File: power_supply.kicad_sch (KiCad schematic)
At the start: 27 parts, among them U7 LM2733XMF

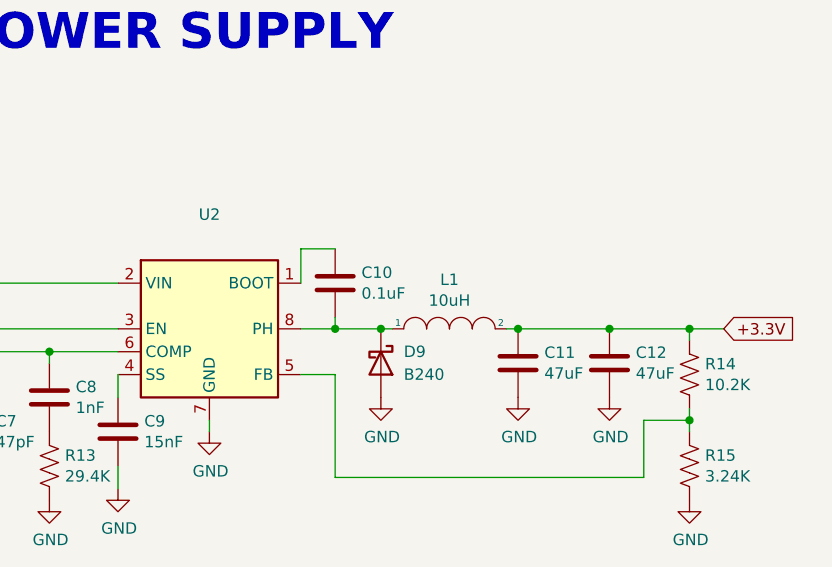
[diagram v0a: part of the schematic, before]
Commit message: Added connector for temperature sensor. Started to route board.
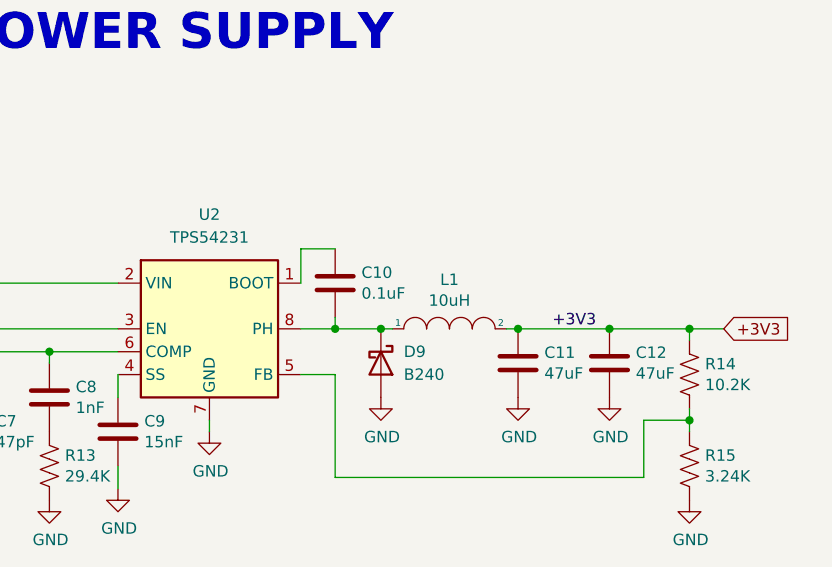
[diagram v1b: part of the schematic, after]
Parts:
- U2: value (none) -> TPS54231; footprint (none) -> Package_SO:SOIC-8_3.9x4.9mm_P1.27mm
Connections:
- net +3.3V renamed +3V3
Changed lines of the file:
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@@
     (effects (font (size 3.9878 3.9878) (thickness 0.7976) bold) (justify left bottom))
   )
-  (global_label "+3.3V" (shape input) (at 209.55 60.96 0) (fields_autoplaced)
+  (label "+3V3" (at 190.5 60.96 0)
+    (effects (font (size 1.27 1.27)) (justify left bottom))
+  )
+  (global_label "+3V3" (shape input) (at 209.55 60.96 0) (fields_autoplaced)
     (effects (font (size 1.27 1.27)) (justify left))
-    (property "Intersheet References" "${INTERSHEET_REFS}" (id 0) (at -6.35 -21.59 0)
-      (effects (font (size 1.27 1.27)) hide)
+    (property "Intersheet References" "${INTERSHEET_REFS}" (id 0) (at 216.9542 60.8806 0)
+      (effects (font (size 1.27 1.27)) (justify left) hide)
     )
   )
@@
     (in_bom yes) (on_board yes) (fields_autoplaced)
     (property "Reference" "U2" (id 0) (at 152.4 48.26 0))
-    (property "Value" "" (id 1) (at 152.4 50.8 0))
-    (property "Footprint" "" (id 2) (at 152.4 60.96 0)
-      (effects (font (size 1.27 1.27)) hide)
-    )
+    (property "Value" "TPS54231" (id 1) (at 152.4 50.8 0))
+    (property "Footprint" "Package_SO:SOIC-8_3.9x4.9mm_P1.27mm" (id 2) (at 152.4 60.96 0)
+      (effects (font (size 1.27 1.27)) hide)
+    )

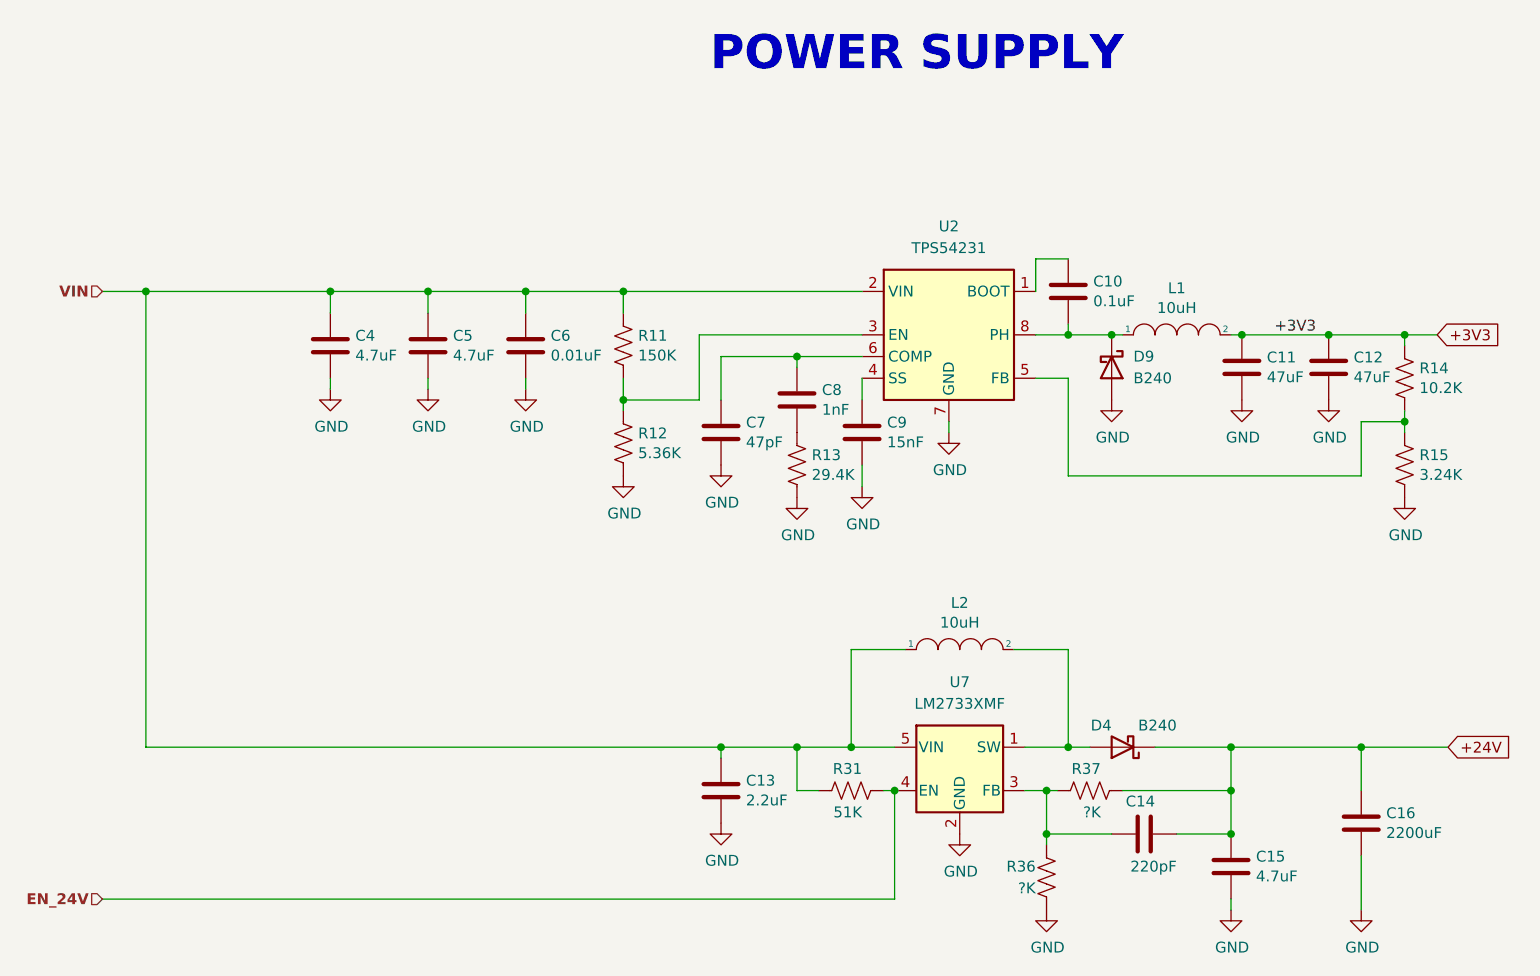
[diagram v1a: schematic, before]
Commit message: Added clamping diode for 24V net.
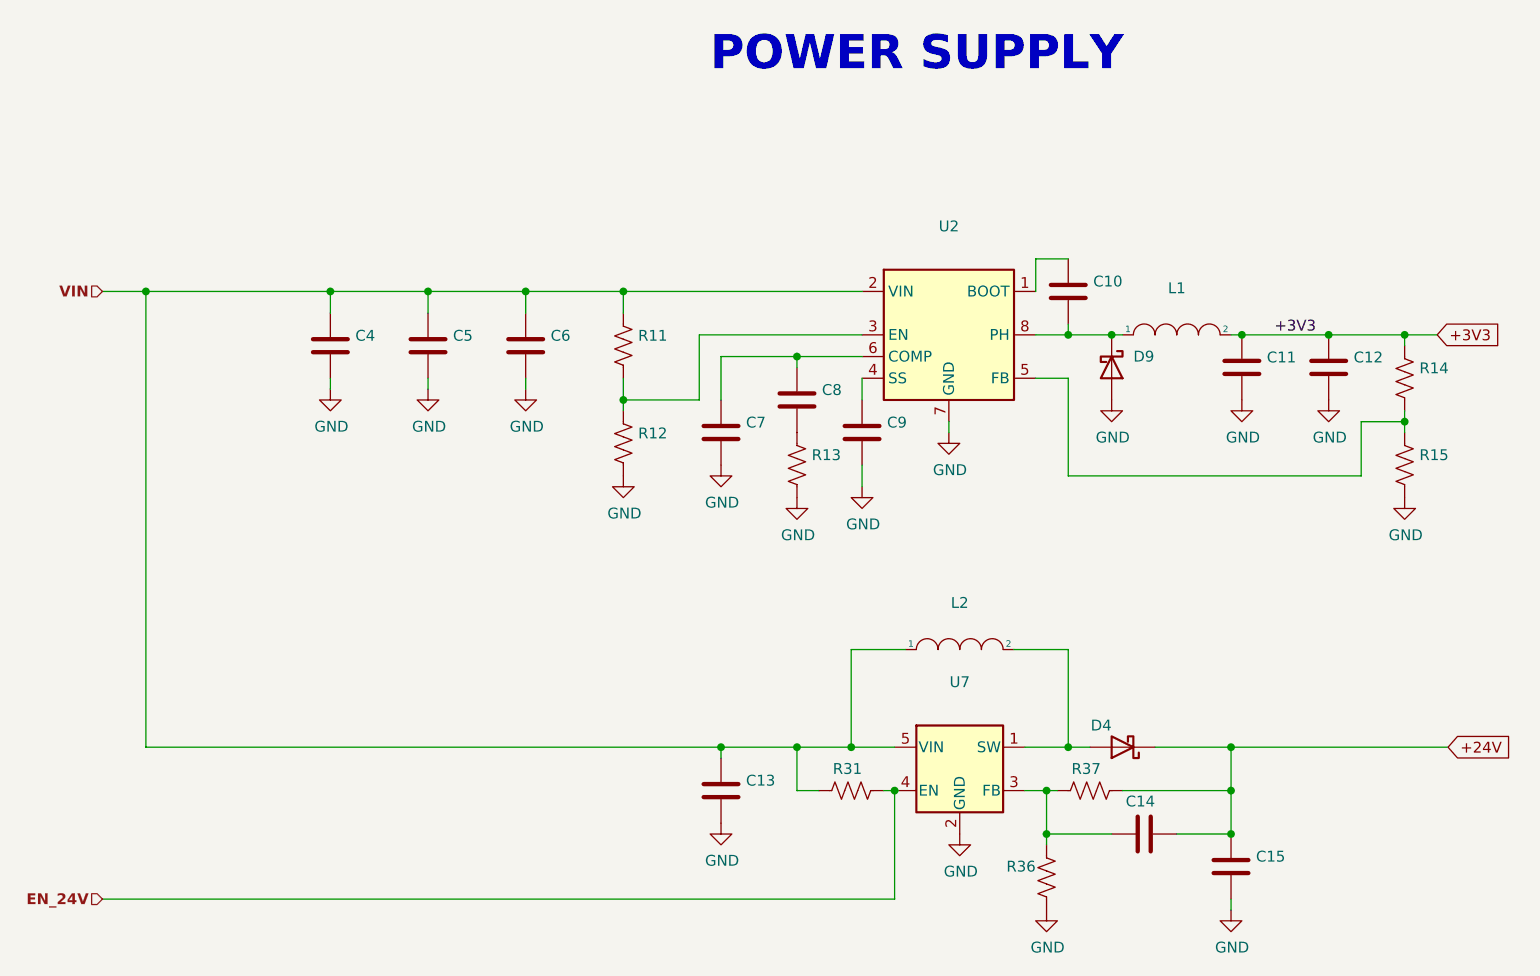
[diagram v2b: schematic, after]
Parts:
- removed C16: 2200uF, Capacitor_SMD:C_0805_2012Metric, symbol Device:C
- C10: value 0.1uF -> (none); footprint Capacitor_SMD:C_0805_2012Metric -> (none)
- C11, C12: value 47uF -> (none); footprint Capacitor_SMD:C_0805_2012Metric -> (none)
- C13: value 2.2uF -> (none); footprint Capacitor_SMD:C_0805_2012Metric -> (none)
- C14: value 220pF -> (none); footprint Capacitor_SMD:C_0805_2012Metric -> (none)
- C15, C4, C5: value 4.7uF -> (none); footprint Capacitor_SMD:C_0805_2012Metric -> (none)
- C6: value 0.01uF -> (none); footprint Capacitor_SMD:C_0805_2012Metric -> (none)
- C7: value 47pF -> (none); footprint Capacitor_SMD:C_0805_2012Metric -> (none)
- C8: value 1nF -> (none); footprint Capacitor_SMD:C_0805_2012Metric -> (none)
- C9: value 15nF -> (none); footprint Capacitor_SMD:C_0805_2012Metric -> (none)
- D4, D9: value B240 -> (none); footprint Diode_SMD:D_SMB -> (none)
- L1, L2: value 10uH -> (none); footprint Inductor_SMD:L_Taiyo-Yuden_NR-50xx -> (none)
- R11: value 150K -> (none); footprint Resistor_SMD:R_0805_2012Metric -> (none)
- R12: value 5.36K -> (none); footprint Resistor_SMD:R_0805_2012Metric -> (none)
- R13: value 29.4K -> (none); footprint Resistor_SMD:R_0805_2012Metric -> (none)
- R14: value 10.2K -> (none); footprint Resistor_SMD:R_0805_2012Metric -> (none)
- R15: value 3.24K -> (none); footprint Resistor_SMD:R_0805_2012Metric -> (none)
- R31: value 51K -> (none); footprint Resistor_SMD:R_0805_2012Metric -> (none)
- R36, R37: value ?K -> (none); footprint Resistor_SMD:R_0805_2012Metric -> (none)
- U2: value TPS54231 -> (none); footprint Package_SO:SOIC-8_3.9x4.9mm_P1.27mm -> (none)
- U7: value LM2733XMF -> (none); footprint Package_TO_SOT_SMD:SOT-23-5 -> (none)

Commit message: Finished initial layout.  Zero DRC errors/warnings.
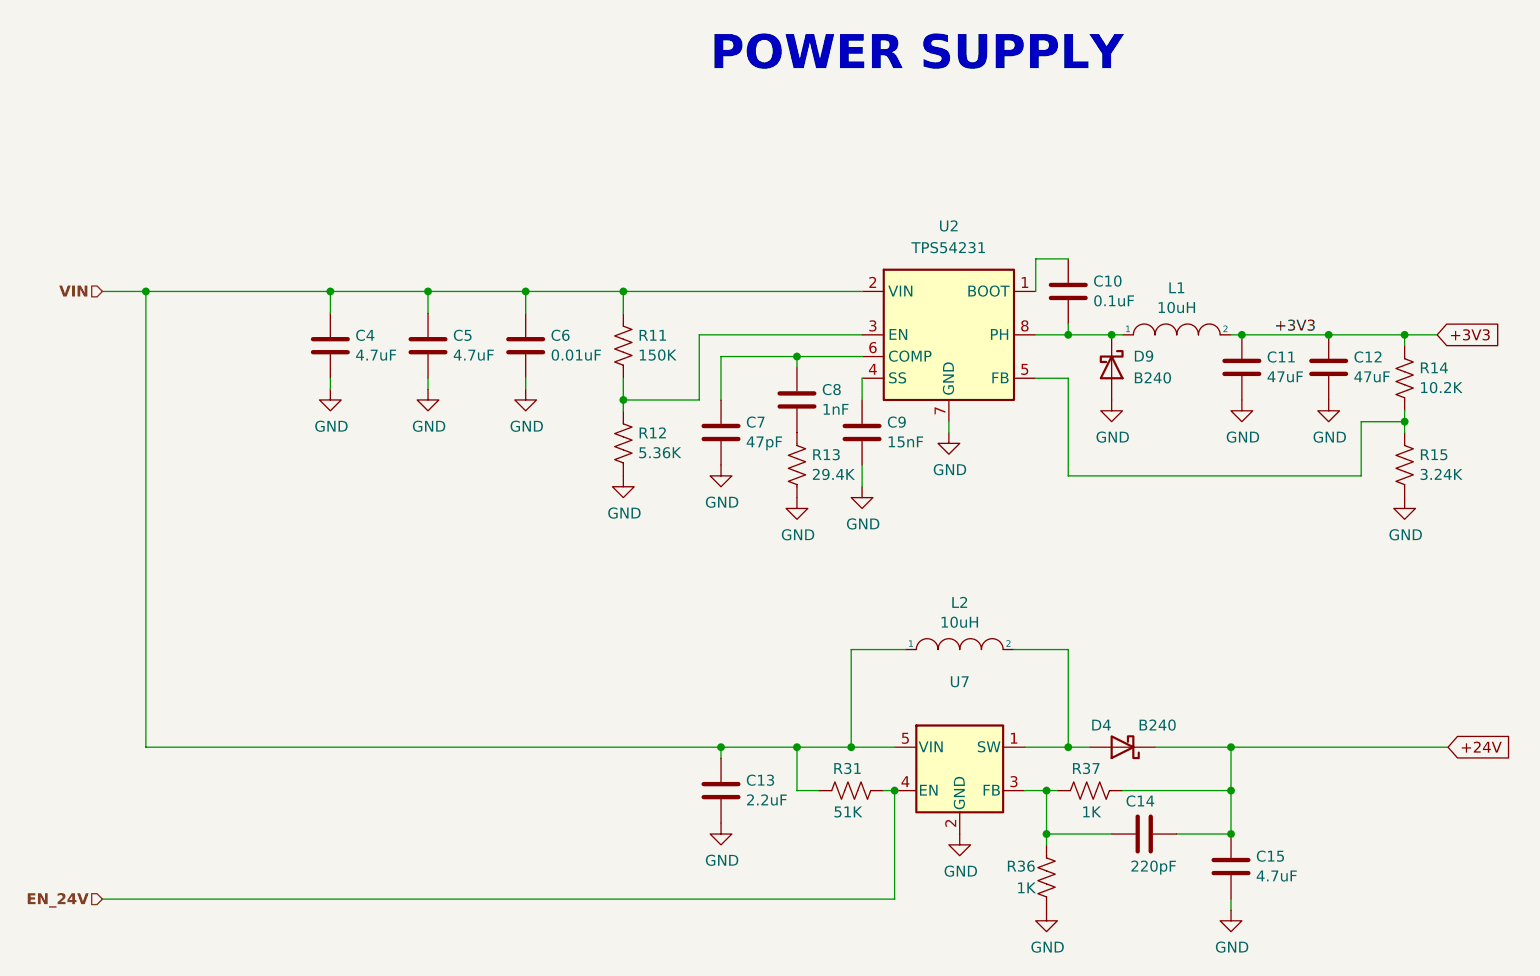
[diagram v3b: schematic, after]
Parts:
- C10: value (none) -> 0.1uF; footprint (none) -> Capacitor_SMD:C_0805_2012Metric
- C11, C12: value (none) -> 47uF; footprint (none) -> Capacitor_SMD:C_0805_2012Metric
- C13: value (none) -> 2.2uF; footprint (none) -> Capacitor_SMD:C_0805_2012Metric
- C14: value (none) -> 220pF; footprint (none) -> Capacitor_SMD:C_0805_2012Metric
- C15, C4, C5: value (none) -> 4.7uF; footprint (none) -> Capacitor_SMD:C_0805_2012Metric
- C6: value (none) -> 0.01uF; footprint (none) -> Capacitor_SMD:C_0805_2012Metric
- C7: value (none) -> 47pF; footprint (none) -> Capacitor_SMD:C_0805_2012Metric
- C8: value (none) -> 1nF; footprint (none) -> Capacitor_SMD:C_0805_2012Metric
- C9: value (none) -> 15nF; footprint (none) -> Capacitor_SMD:C_0805_2012Metric
- D4, D9: value (none) -> B240; footprint (none) -> Diode_SMD:D_SMB
- L1, L2: value (none) -> 10uH; footprint (none) -> Inductor_SMD:L_Taiyo-Yuden_NR-50xx
- R11: value (none) -> 150K; footprint (none) -> Resistor_SMD:R_0805_2012Metric
- R12: value (none) -> 5.36K; footprint (none) -> Resistor_SMD:R_0805_2012Metric
- R13: value (none) -> 29.4K; footprint (none) -> Resistor_SMD:R_0805_2012Metric
- R14: value (none) -> 10.2K; footprint (none) -> Resistor_SMD:R_0805_2012Metric
- R15: value (none) -> 3.24K; footprint (none) -> Resistor_SMD:R_0805_2012Metric
- R31: value (none) -> 51K; footprint (none) -> Resistor_SMD:R_0805_2012Metric
- R36, R37: value (none) -> 1K; footprint (none) -> Resistor_SMD:R_0805_2012Metric
- U2: value (none) -> TPS54231; footprint (none) -> Package_SO:SOIC-8_3.9x4.9mm_P1.27mm
- U7: footprint (none) -> Package_TO_SOT_SMD:SOT-23-5

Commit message: Added DHT11 footprint. Updated feedback resistor values for regulator circuit. Created gerber and drill files for version 1.
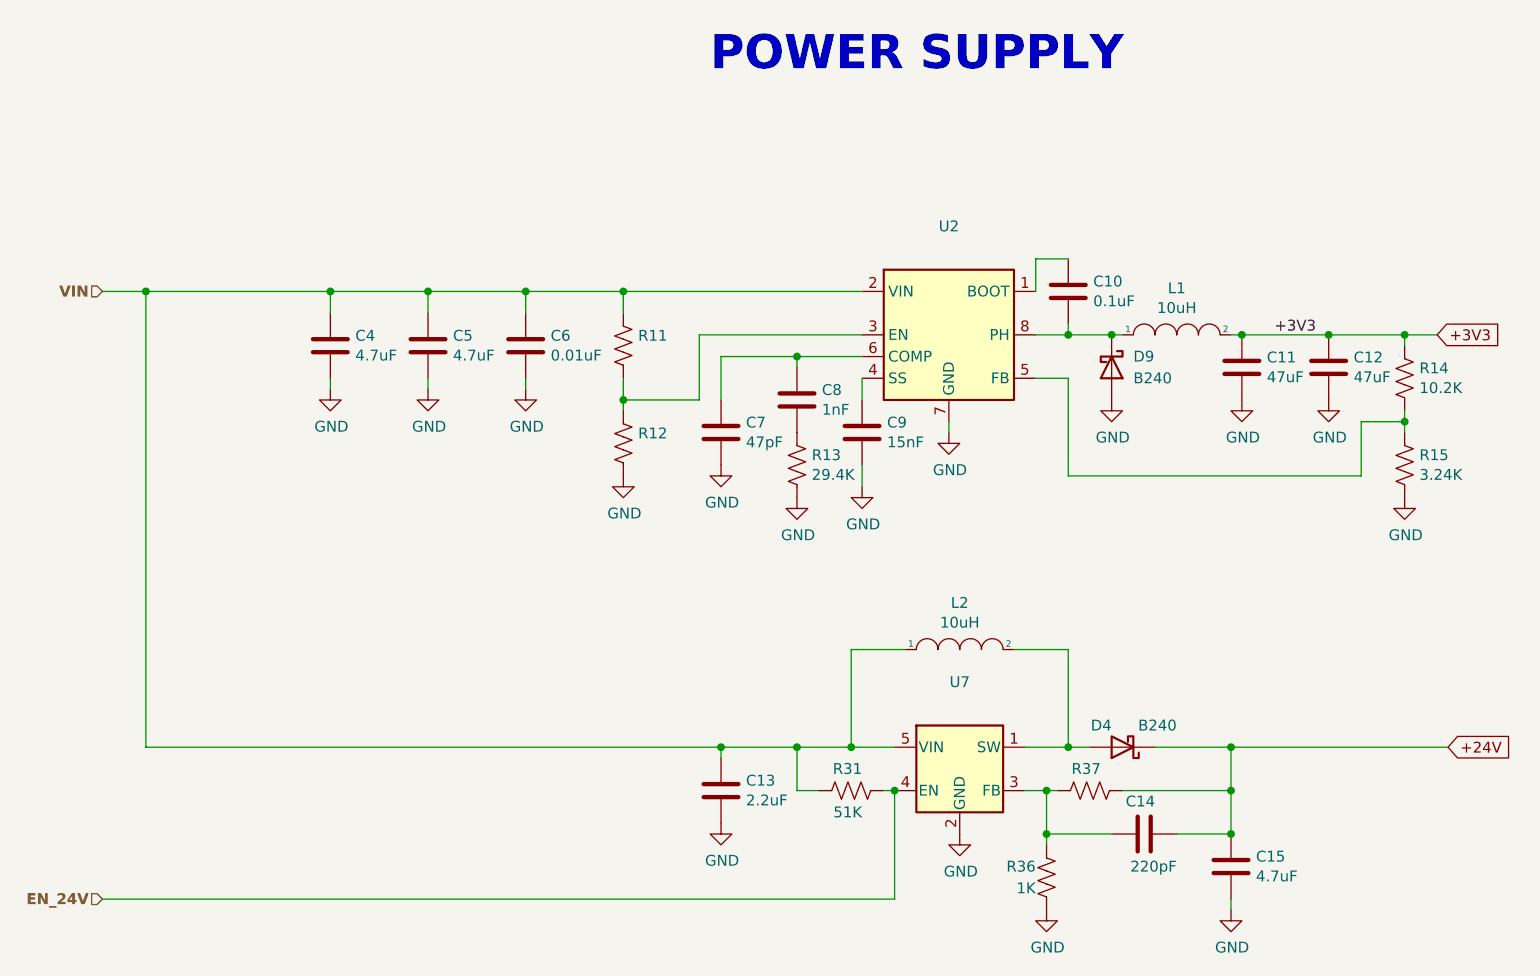
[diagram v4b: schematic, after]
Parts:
- R11: value 150K -> (none)
- R12: value 5.36K -> (none); footprint Resistor_SMD:R_0805_2012Metric -> (none)
- R37: value 1K -> (none); footprint Resistor_SMD:R_0805_2012Metric -> (none)
- U2: value TPS54231 -> (none)
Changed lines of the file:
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@@
       (effects (font (size 1.27 1.27)) (justify left))
     )
-    (property "Value" "150K" (id 1) (at 116.0272 63.373 0)
+    (property "Value" "" (id 1) (at 116.0272 63.373 0)
       (effects (font (size 1.27 1.27)) (justify left))
     )
@@
       (effects (font (size 1.27 1.27)) (justify left))
     )
-    (property "Value" "5.36K" (id 1) (at 116.0272 74.803 0)
-      (effects (font (size 1.27 1.27)) (justify left))
-    )
-    (property "Footprint" "Resistor_SMD:R_0805_2012Metric" (id 2) (at 115.316 73.914 90)
+    (property "Value" "" (id 1) (at 116.0272 74.803 0)
+      (effects (font (size 1.27 1.27)) (justify left))
+    )
+    (property "Footprint" "" (id 2) (at 115.316 73.914 90)
       (effects (font (size 1.27 1.27)) hide)
     )
@@
     (in_bom yes) (on_board yes) (fields_autoplaced)
     (property "Reference" "U2" (id 0) (at 152.4 48.26 0))
-    (property "Value" "TPS54231" (id 1) (at 152.4 50.8 0))
+    (property "Value" "" (id 1) (at 152.4 50.8 0))
     (property "Footprint" "Package_SO:SOIC-8_3.9x4.9mm_P1.27mm" (id 2) (at 152.4 60.96 0)
       (effects (font (size 1.27 1.27)) hide)
@@
       (effects (font (size 1.27 1.27)) (justify left))
     )
-    (property "Value" "1K" (id 1) (at 170.18 116.84 90)
-      (effects (font (size 1.27 1.27)) (justify left))
-    )
-    (property "Footprint" "Resistor_SMD:R_0805_2012Metric" (id 2) (at 169.164 113.284 90)
-      (effects (font (size 1.27 1.27)) hide)
-    )
+    (property "Value" "" (id 1) (at 170.18 116.84 90)
+      (effects (font (size 1.27 1.27)) (justify left))
+    )
+    (property "Footprint" "" (id 2) (at 169.164 113.284 90)
+      (effects (font (size 1.27 1.27)) hide)
+    )
